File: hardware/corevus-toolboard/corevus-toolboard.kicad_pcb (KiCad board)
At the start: 4 copper layers, 49.8 x 24.2 mm, 83 parts, among them J1 MF3, J10 1x3P, J2 XH, J3 MF3, J4 XH, J5 XH, J6 XH, J7 XH, J8 pinheader, J9 XH, Q2 NMOS, Q3 AO3401A, Q4 AO3400, Q5 AO3400, SW1 RST, U1 LIS2DE12, U2 TPS54302, U3 STM32G431KBU3, U4 TMC2209-LA, U5 74LVC1G17, U6 SPX3819M5-L-3-3, Y1 XRCGB25

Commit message: updated with h723 fix workaround info
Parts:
- C2, C3: value 15pF -> 10pF
- R12: value xkΩ -> 630Ω
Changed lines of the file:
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@@
         (effects (font (size 0.6 0.6) (thickness 0.15)) (justify mirror))
     )
-    (fp_text value "15pF" (at 0 -0.1) (layer "B.Fab")
+    (fp_text value "10pF" (at 0 -0.1) (layer "B.Fab")
         (effects (font (size 0.25 0.15) (thickness 0.025)) (justify mirror))
     )
@@
         (effects (font (size 0.6 0.6) (thickness 0.15)) (justify mirror))
     )
-    (fp_text value "15pF" (at 0 -0.1 90) (layer "B.Fab")
+    (fp_text value "10pF" (at 0 -0.1 90) (layer "B.Fab")
         (effects (font (size 0.25 0.15) (thickness 0.025)) (justify mirror))
     )
@@
         (effects (font (size 1 1) (thickness 0.15)) (justify mirror))
     )
-    (fp_text value "TPS54302" (at 0 -2.4 90) (layer "B.Fab")
+    (fp_text value "TPS54302" (at 0 0 90) (layer "B.Fab")
         (effects (font (size 1 1) (thickness 0.15)) (justify mirror))
     )
@@
         (effects (font (size 0.6 0.6) (thickness 0.15)) (justify mirror))
     )
-    (fp_text value "xkΩ" (at 0 -0.1 90) (layer "B.Fab")
+    (fp_text value "630Ω" (at 0 -0.1 90) (layer "B.Fab")
         (effects (font (size 0.25 0.15) (thickness 0.025)) (justify mirror))
     )
@@
         (effects (font (size 1 1) (thickness 0.15)) (justify mirror))
     )
-    (fp_text value "TMC2209-LA" (at 0 -3.8 90) (layer "B.Fab")
-        (effects (font (size 1 1) (thickness 0.15)) (justify mirror))
-    )
+    (fp_text value "TMC2209-LA" (at 0 -1.5 90) (layer "B.Fab")
+        (effects (font (size 1 1) (thickness 0.15)) (justify mirror))
+    )

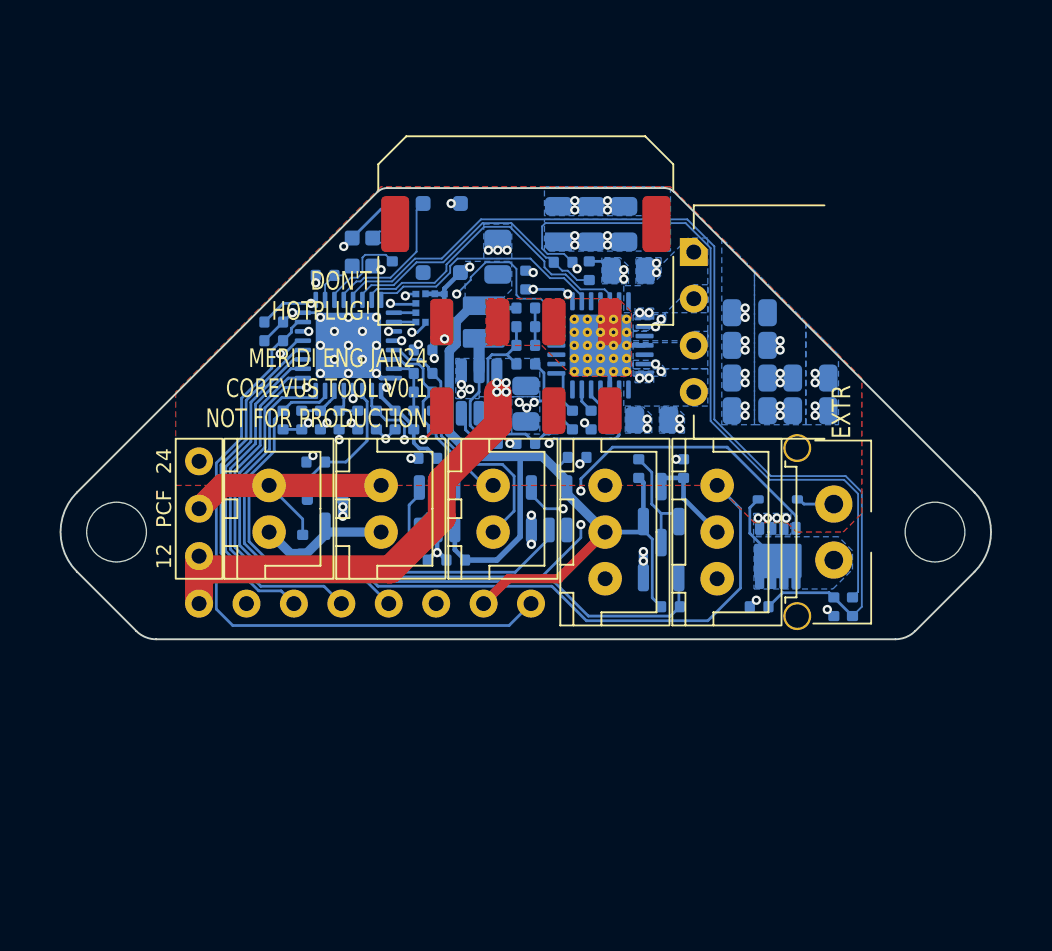
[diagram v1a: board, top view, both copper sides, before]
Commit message: corevus toolboard v0.2 release (working), corevus-g v0.2 release (very much not working), m++ v0.1 (not working, needs a lot of bodges)
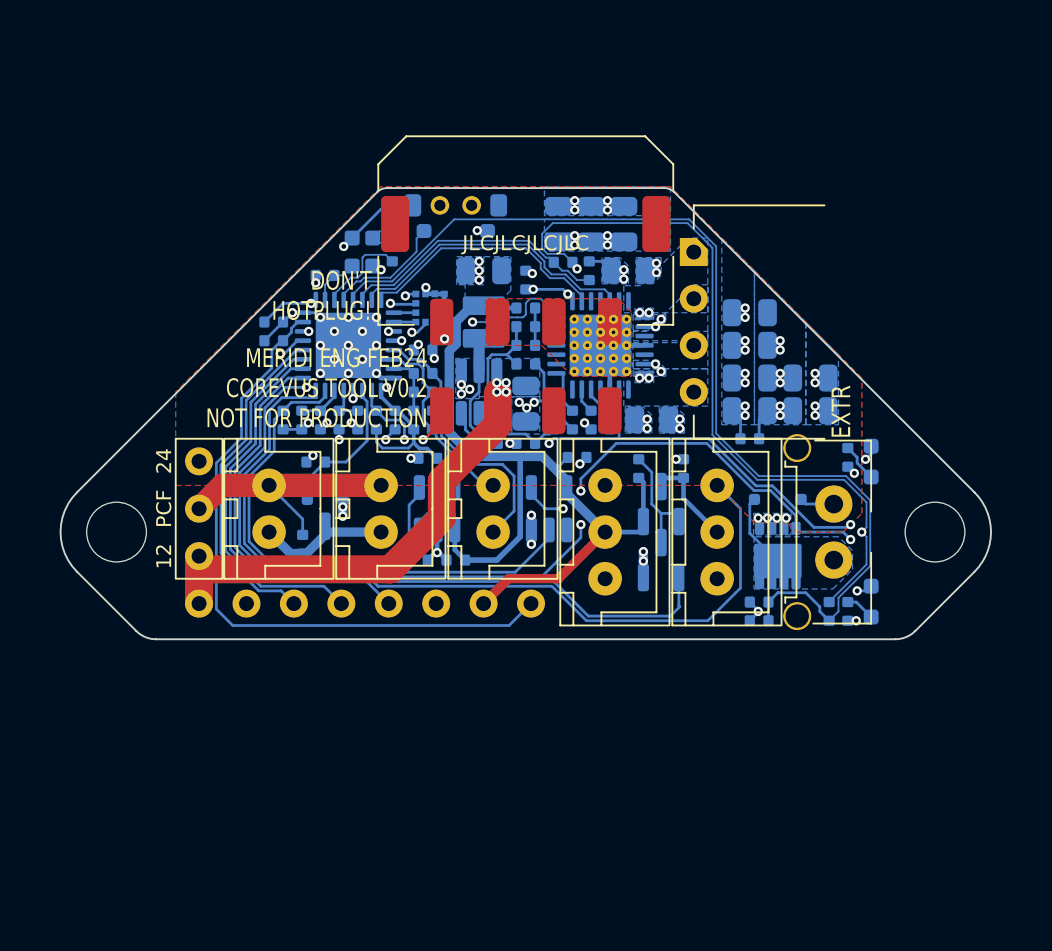
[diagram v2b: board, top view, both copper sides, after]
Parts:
- added D2: Red, corevus:XL1606, B.Cu at (18.5, 3.75)
- added D3: Grn, corevus:XL1606, B.Cu at (18.5, -3.75)
- added R20: 510kΩ, AlphaLib:0402R, B.Cu at (12.0, -5.00)
- added R21: 470Ω, AlphaLib:0402R, B.Cu at (17.2, -4.00)
- FB1: value GZsth -> GZ1005
- R1: value 2.2kΩ -> 1kΩ
- R10: value 13.3kΩ -> 20kΩ
- R11: value 100kΩ -> 150kΩ
- R12: value 630Ω -> 1kΩ
- R8: value 500kΩ -> 510kΩ
- SW1: footprint corevus:ShouHan_TS3315A -> corevus:ShouHan_TS24CA
- moved R1 9.50 mm to (17.2, 4.25), turned to 90 degrees
- moved C30 4.07 mm to (12.5, 4.75), turned to 0 degrees
- moved SW1 1.90 mm to (-3.75, -17.5), turned to 180 degrees
- moved R17 1.27 mm to (16.2, 4.25)
- moved C33 1.06 mm to (-2.25, -14.0), turned to 180 degrees
- moved TH2 0.25 mm to (12.5, 3.75)
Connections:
- R1 pad 1: /F0 -> GND
- R1 pad 2: +5V -> Net-(D2-K)
- R18 pad 2: GND -> +3.3V
- SW1 pad 1: GND -> /~{Reset}
- SW1 pad 2: /~{Reset} -> GND
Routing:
- net /~{En}: track 18.5 -> 36.5 mm, vias 2 -> 4
- net +3.3V: track 75.0 -> 84.2 mm, vias 6 -> 8
- net /H0_Gate: track 18.8 -> 25.9 mm, vias 2 -> 4
- net +5V: track 50.0 -> 45.5 mm
- net /UART: track 19.5 -> 16.7 mm
- net Net-(D3-K): track 0.00 -> 2.07 mm
- net +24V: track 2.55 -> 4.23 mm
- net Net-(D2-K): track 0.00 -> 1.58 mm
- net /_{FET}Therm: track 52.9 -> 54.4 mm
- net /~{Reset}: track 7.88 -> 6.43 mm
- net /Dir: track 16.8 -> 15.8 mm
- net /_{Motor}Therm: track 15.3 -> 14.6 mm
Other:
- board text added: "DFU"
- board text added: "JLCJLCJLCJLC"
- board text added: "MERIDI ENG FEB24 COREVUS TOOL V0.2 NOT FOR PRODUCTION"
- board text added: "RST"
- board text removed: "BOOT"
- board text removed: "MERIDI ENG JAN24 COREVUS TOOL V0.1 NOT FOR PRODUCTION"
- board text removed: "←RST"

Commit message: v0.3 toolboard nearing completion (just need to make the production files), also made panelization test board
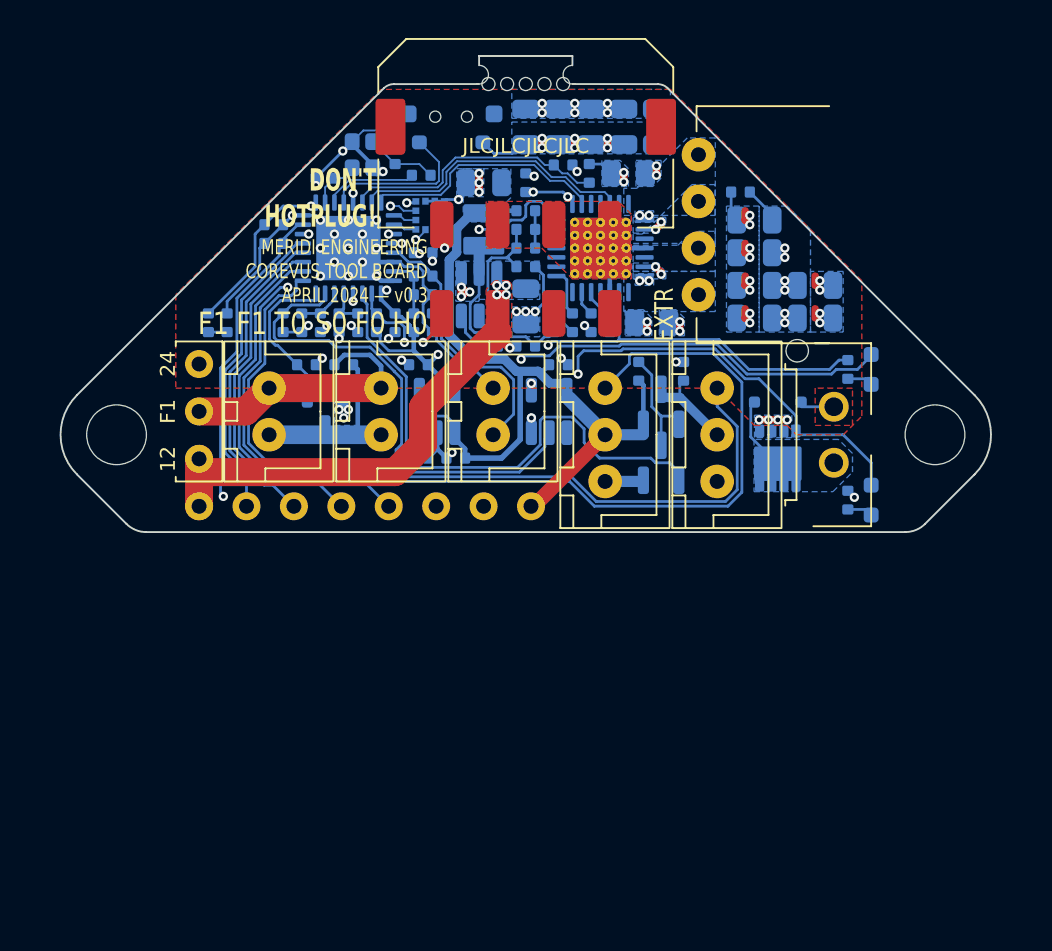
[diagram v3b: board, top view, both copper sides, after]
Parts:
- removed TH2: 10kΩ 3950K, AlphaLib:0402R
- added D4: Grn, AlphaLib:0402LED, B.Cu at (-17.0, -11.2)
- added REF**: mousebite-0.7x5, corevus:mousebite-0.7x5, F.Cu at (0.00, -24.0)
- C10: value 1μF -> 100nF
- C24, C25: value 1nF -> 100pF
- C26: value 1µF -> 2.2µF
- C30: value 100nF -> 4.7µF 50V; footprint AlphaLib:0402C -> Capacitor_SMD:C_0805_2012Metric
- D1: value 5819 -> 4148
- R17: value 4.7kΩ -> 2.2kΩ
- R21: value 470Ω -> 2.2kΩ
- moved R17 35.8 mm to (-16.0, -11.2), turned to -90 degrees
- moved C30 29.3 mm to (0.00, -21.7), turned to -90 degrees
- moved R20 13.2 mm to (11.5, -18.2)
- moved C23 9.86 mm to (-9.75, -8.96), turned to 180 degrees
- moved R1 5.96 mm to (17.2, -1.71), turned to -90 degrees
- moved C1 5.46 mm to (-3.75, -3.96)
- moved C31 5.46 mm to (-5.75, -3.96)
- moved D2 5.46 mm to (18.5, -1.71)
- moved R14 5.24 mm to (-11.7, -8.96), turned to 0 degrees
- moved J4 5.22 mm to (9.25, -16.5)
- moved J8 5.21 mm to (-17.5, -1.38)
- moved U6 5.21 mm to (-4.75, -6.46)
- moved R16 5.21 mm to (2.00, -19.7)
- moved C10 5.21 mm to (8.45, -8.61)
- moved C24 5.21 mm to (-12.0, -11.2)
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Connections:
- C30 pad 1: GND -> +24V
- C30 pad 2: /_{FET}Therm -> GND
- J8 pad 2: unconnected-(J8-Pin_2-Pad2) -> /PB6
- J8 pad 7: +5V -> /BOOT0
- J8 pad 8: /BOOT0 -> +5V
- R17 pad 1: /_{FET}Therm -> GND
- R17 pad 2: +3.3V -> Net-(D4-K)
- U3 pad 19: /F1 -> /F0
- U3 pad 24: /S0 -> /F1
- U3 pad 29: /F0 -> /PB6
- U3 pad 30: /INT1 -> /S0
- U3 pad 5: /_{FET}Therm -> /INT1
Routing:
- net /_{FET}Therm: track 54.4 -> 0.00 mm
- net /S0: track 33.7 -> 56.7 mm, vias 1 -> 2
- net GND: track 39.0 -> 56.4 mm, vias 70 -> 68
- net /PB6: track 0.00 -> 16.5 mm
- net /F0: track 41.4 -> 28.7 mm, vias 2 -> 0
- net +3.3V: track 84.2 -> 72.4 mm
- net /PCF_V+: track 13.7 -> 20.4 mm
- net /~{En}: track 36.5 -> 31.8 mm, vias 4 -> 2
- net /BOOT0: track 35.2 -> 31.1 mm, vias 0 -> 1
- net Net-(J6-Pin_1): track 7.35 -> 10.3 mm
- net /F0_FG: track 46.5 -> 43.8 mm
- net +5V: track 45.5 -> 43.3 mm
- net /H0: track 28.2 -> 26.1 mm
- net /~{Reset}: track 6.43 -> 8.44 mm
- net /H0_Gate: track 25.9 -> 24.0 mm, vias 4 -> 2
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- added copper zone on F.Cu, net +12V
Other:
- board size 49.8 x 24.2 mm -> 49.8 x 25.5 mm
- board text added: "F0"
- board text added: "F1"
- board text added: "H0"
- board text added: "MERIDI ENGINEERING COREVUS TOOL BOARD APRIL 2024 — v0.3"
- board text added: "S0"
- board text added: "T0"
- board text removed: "MERIDI ENG FEB24 COREVUS TOOL V0.2 NOT FOR PRODUCTION"
- board text removed: "PCF"
- board text removed: "meridi engineering"

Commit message: finished production data for toolboard v0.3, just waiting on parts eeeeeeee
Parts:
- removed REF**: mousebite-0.7x5, corevus:mousebite-0.7x5
- C24, C25: value 100pF -> 10pF
- C28: value 75pF -> 68pF
- C32: value xµF 25V -> 10µF 25V
- C33: value xµF -> 10µF
- R15: value 50Ω -> 51Ω
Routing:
- net GND: track 56.4 -> 57.3 mm
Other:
- board size 49.8 x 25.5 mm -> 49.8 x 24 mm

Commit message: should be up to date for cvg v0.6 and latest protected drivers
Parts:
- removed C24, C25: 10pF, AlphaLib:0402C
- C11, C12, C13, C26, C27, C4, C5: value 2.2µF -> 1µF
- C29: value 100nF -> 1µF 25V
- C9: value 100nF 50V -> 22nF 50V
- R1: value 1kΩ -> 4.7kΩ
- U5: value 74LVC1G17 -> MCP1416
- moved D3 23.3 mm to (5.95, 10.9)
- moved R21 23.3 mm to (4.70, 10.9)
- moved R1 21.3 mm to (-1.39, 8.66), turned to 180 degrees
- moved R7 21.1 mm to (16.5, 9.75)
- moved C10 20.3 mm to (19.8, 8.25)
- moved R16 14.3 mm to (-11.8, -23.5), turned to -90 degrees
- moved Q5 12.6 mm to (17.2, 4.00)
- moved Q3 12.5 mm to (13.8, 4.00)
- moved C7 9.93 mm to (1.50, -19.2), turned to -90 degrees
- moved C27 9.75 mm to (-14.3, -19.1)
- moved R9 9.21 mm to (-3.00, -19.2)
- moved U1 8.27 mm to (-12.8, -13.8), turned to 180 degrees
- moved D4 8.14 mm to (-17.1, -19.3)
- moved R17 8.14 mm to (-16.1, -19.3)
- moved R8 7.88 mm to (-3.00, -17.2), turned to 90 degrees
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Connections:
- net /USB_D+ renamed /D+'
- net /USB_D- renamed /D-'
- net Net-(J3-Pin_1) renamed /D-
- net Net-(J3-Pin_5) renamed /D+
- C29 pad 1: +5V -> +12V
- D2 pad 2: /H0_Gate -> /H0
- J5 pad 1: /T0 -> VSSA
- J5 pad 2: VSSA -> /T0
- J8 pad 2: /PB6 -> /PA4
- J8 pad 3: /PB5 -> /PA5
- J8 pad 4: /PB4 -> /PA6
- J8 pad 5: /PB3 -> /PA7
- U1 pad 1: /SCK -> /SPI1_SCK
- U1 pad 11: /INT2 -> unconnected-(U1-INT2-Pad11)
- U1 pad 12: /INT1 -> unconnected-(U1-INT1-Pad12)
- U1 pad 3: /MISO -> /SPI1_MISO
- U1 pad 4: /MOSI -> /SPI1_MOSI
- U3 pad 10: /SCK -> /PA5
- U3 pad 11: /MISO -> /PA6
- U3 pad 12: /MOSI -> /PA7
- U3 pad 20: /UART -> /INT1
- U3 pad 25: /F0_FG -> /ACCEL_CS
- U3 pad 26: /PB3 -> /SPI1_SCK
- U3 pad 27: /PB4 -> /SPI1_MISO
- U3 pad 28: /PB5 -> /SPI1_MOSI
- U3 pad 29: /PB6 -> unconnected-(U3-PB6-Pad29)
- U3 pad 5: /INT1 -> /UART
- U3 pad 6: /_{Motor}Therm -> /Dir
- U3 pad 7: /Dir -> /_{Motor}Therm
- U3 pad 9: /ACCEL_CS -> /PA4
- U5 pad 1: unconnected-(U5-NC-Pad1) -> GND
- U5 pad 2: /H0 -> +12V
- U5 pad 3: GND -> /H0
- U5 pad 4: /H0_Gate -> GND
- U5 pad 5: +5V -> /H0_Gate
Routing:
- net /S0: track 56.7 -> 0.25 mm, vias 2 -> 0
- net +3.3V: track 72.0 -> 22.1 mm, vias 8 -> 2
- net /F0_FG: track 43.8 -> 0.00 mm
- net /F0: track 28.7 -> 0.31 mm
- net +5V: track 43.3 -> 15.8 mm
- net /H0: track 26.1 -> 1.38 mm
- net /PB3: track 20.5 -> 0.00 mm
- net /PB4: track 18.8 -> 0.00 mm
- net /PB5: track 17.1 -> 0.00 mm
- net /PB6: track 16.5 -> 0.00 mm
- net /H0_Gate: track 24.0 -> 9.29 mm, vias 2 -> 0
- net /D-: track 9.07 -> 0.00 mm, vias 2 -> 0
- net /T0: track 14.8 -> 5.82 mm
- net /UART: track 16.7 -> 25.5 mm, vias 2 -> 1
- net /F1: track 8.04 -> 0.46 mm
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- removed copper zone on B.Cu, net +12V
- removed copper zone on B.Cu, net +5V
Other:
- board size 49.8 x 24 mm -> 49.8 x 24.2 mm

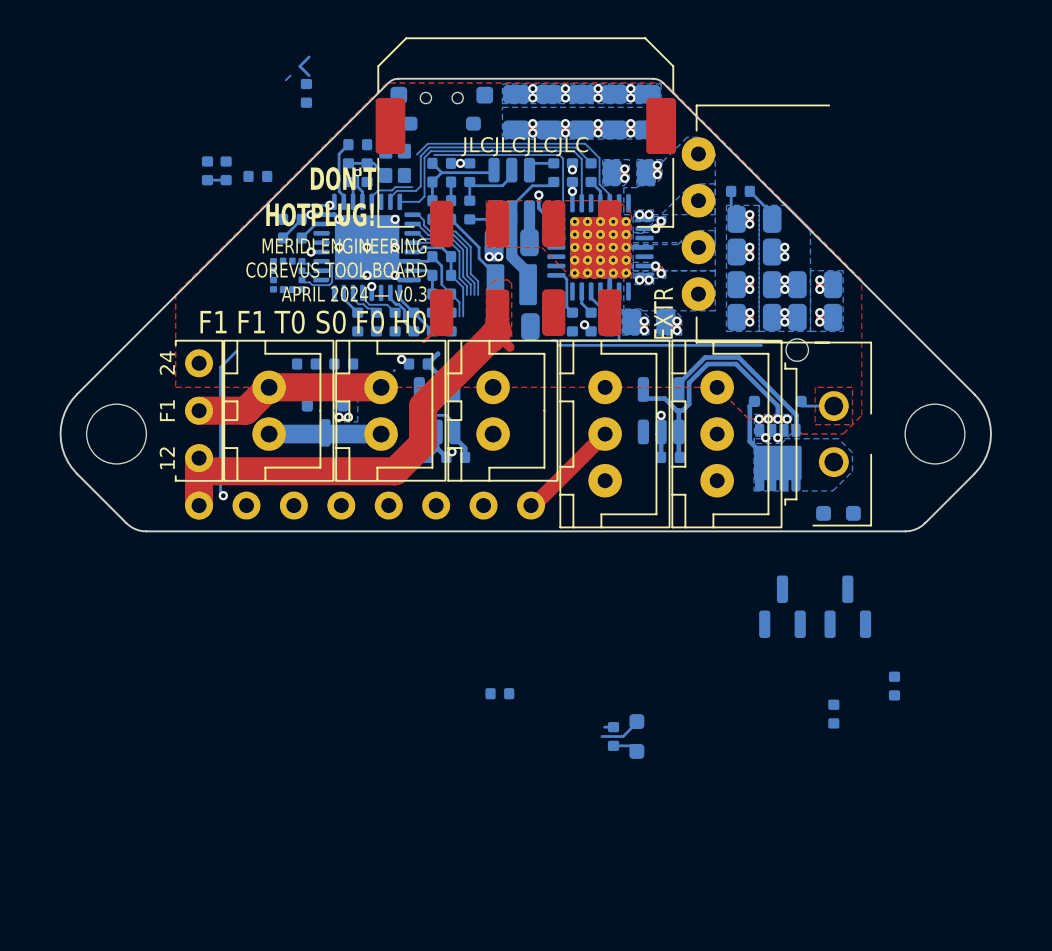
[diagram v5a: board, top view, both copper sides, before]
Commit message: Added details on fan / motor voltage selection
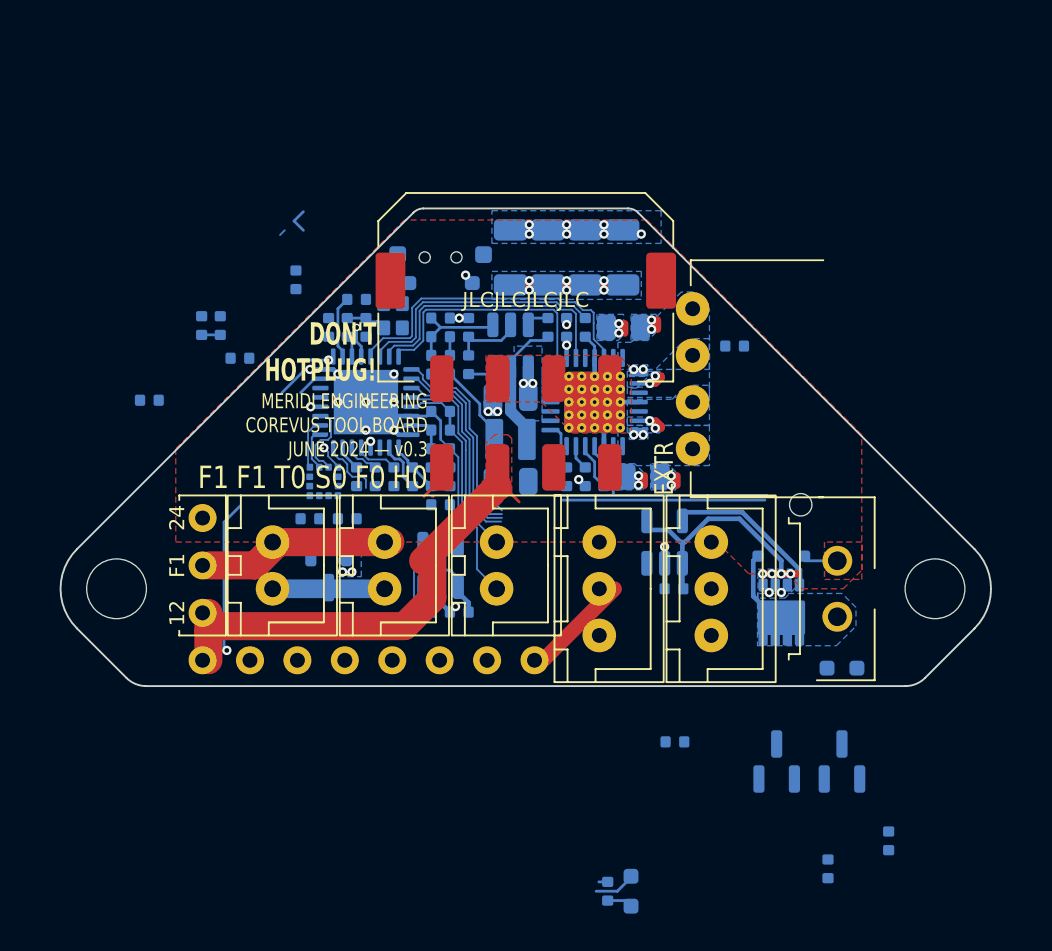
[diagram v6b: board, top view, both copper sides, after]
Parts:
- removed C18, C19, C20, C21, C22, C30, C6: 4.7µF 50V, Capacitor_SMD:C_0805_2012Metric
- C14, C15, C16, C17: value 4.7µF 50V -> 10µF 50V; footprint Capacitor_SMD:C_0805_2012Metric -> Capacitor_SMD:C_1206_3216Metric
- moved R2 11.6 mm to (-20.2, -7.06)
- moved U1 11.2 mm to (-10.8, -2.71), turned to -90 degrees
- moved R16 10.0 mm to (-12.3, -13.5)
- moved R1 9.72 mm to (7.99, 11.2)
- moved C27 8.93 mm to (-10.6, -11.0), turned to 90 degrees
- moved SW1 8.54 mm to (-4.56, -14.7)
- moved D3 8.29 mm to (5.64, 19.2)
- moved C9 8.29 mm to (4.19, -2.96)
- moved D4 8.29 mm to (-17.4, -11.1)
- moved R21 8.29 mm to (4.39, 19.2)
- moved C4 8.29 mm to (2.19, -2.96)
- moved C5 8.29 mm to (2.19, -11.0)
- moved C7 8.29 mm to (1.19, -11.0)
- moved J2 8.29 mm to (9.94, 3.04)
- moved J4 8.29 mm to (8.94, -8.21)
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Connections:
- U3 pad 29: unconnected-(U3-PB6-Pad29) -> /F0_FG
- U3 pad 5: /UART -> /Dir
- U3 pad 6: /Dir -> /_{Motor}Therm
- U3 pad 7: /_{Motor}Therm -> /Step
- U3 pad 8: /Step -> /UART
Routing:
- net GND: track 60.6 -> 35.3 mm, vias 44 -> 32
- net /D+: track 15.5 -> 1.99 mm
- net /UART: track 25.5 -> 14.0 mm, vias 1 -> 0
- net /~{En}: track 25.6 -> 17.2 mm
- net /BOOT0: track 24.3 -> 16.2 mm, vias 1 -> 0
- net +12V: track 31.0 -> 38.6 mm, vias 3 -> 4
- net VSSA: track 6.77 -> 13.7 mm
- net /INT1: track 5.80 -> 0.00 mm
- net /PA7: track 5.20 -> 10.1 mm
- net /T0: track 5.82 -> 10.5 mm
- net /PA6: track 5.66 -> 10.3 mm
- net /PA5: track 6.11 -> 10.4 mm
- net /Dir: track 13.3 -> 17.3 mm
- net /F1: track 0.46 -> 3.78 mm
- net +3.3V: track 22.1 -> 19.5 mm
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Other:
- board size 49.8 x 24.2 mm -> 49.8 x 25.6 mm
- board text added: "MERIDI ENGINEERING COREVUS TOOL BOARD JUNE 2024 — v0.3"
- board text removed: "MERIDI ENGINEERING COREVUS TOOL BOARD APRIL 2024 — v0.3"
